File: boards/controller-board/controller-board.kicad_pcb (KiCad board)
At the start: 2 copper layers, 130 x 115 mm, 213 parts, among them IC10 A6214KLKTR-T, IC11 A6214KLKTR-T, IC12 A6214KLKTR-T, IC13 A6214KLKTR-T, IC2 A6214KLKTR-T, IC3 A6214KLKTR-T, IC4 A6214KLKTR-T, IC5 A6214KLKTR-T, IC6 A6214KLKTR-T, IC7 A6214KLKTR-T, IC8 A6214KLKTR-T, IC9 A6214KLKTR-T, J1 Conn_01x02, J2 Conn_01x02, J3 Conn_01x02, J4 Conn_01x02, J5 Conn_01x03, J6 Conn_01x02, Q1 PMV45EN, Q2 Goford_G11S_20V_11A, SW1 EG1271, U1 LTC3624, U2 ADS1015IRUGR, U3 ADS1015IRUGR, U4 RPi_Pico, U5 MCP4728

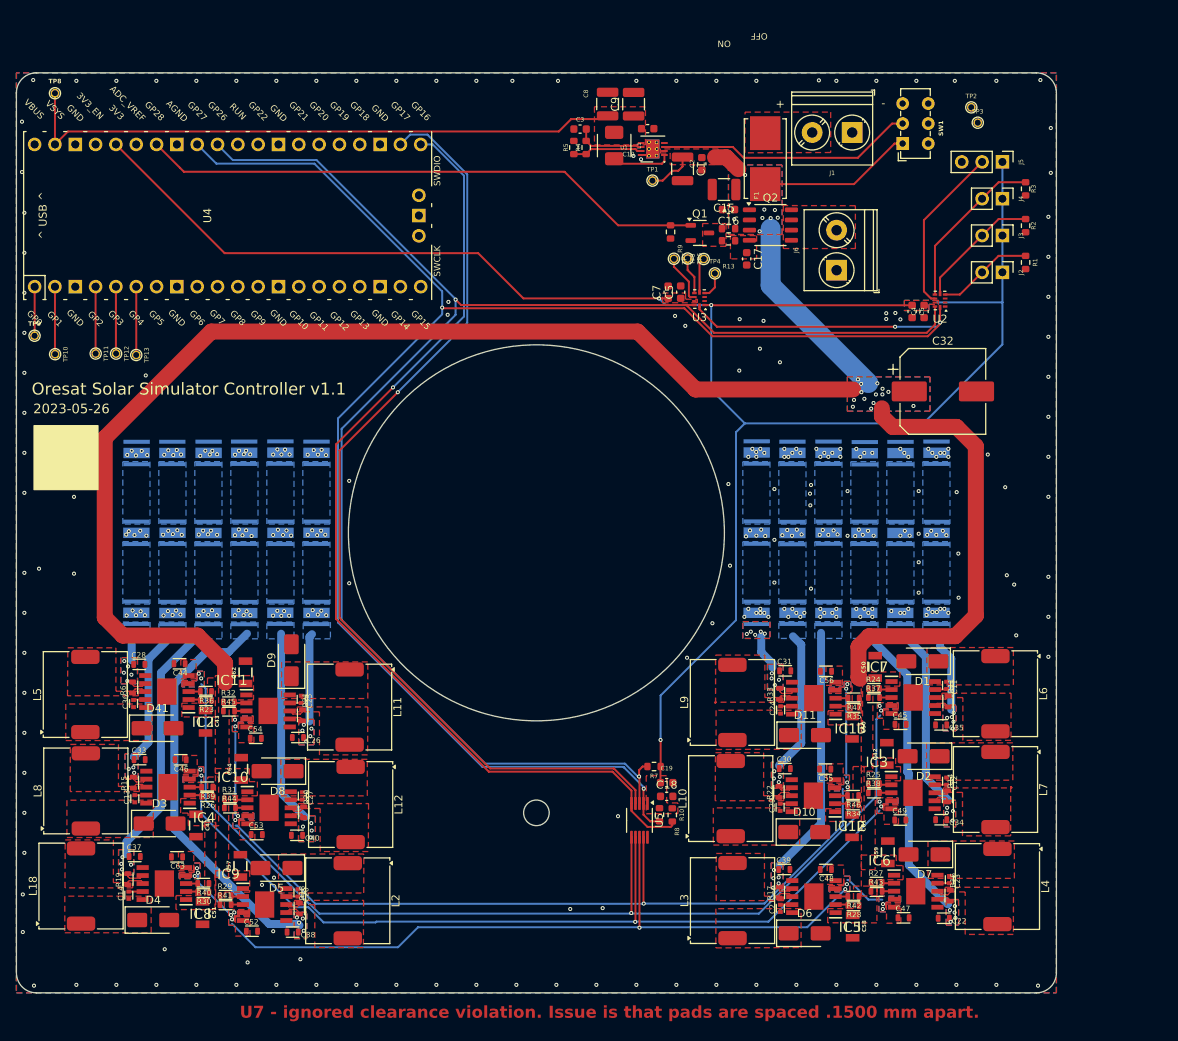
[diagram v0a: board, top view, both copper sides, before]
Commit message: added pull-down resistor to ADIM pins on LED drivers, completed BOM, reorganized schematic, switched 10k resistors and thermistors, added datasheets, split 12V pwr supply and added additional fuse, changed main pwr input connector to one with higher current rating
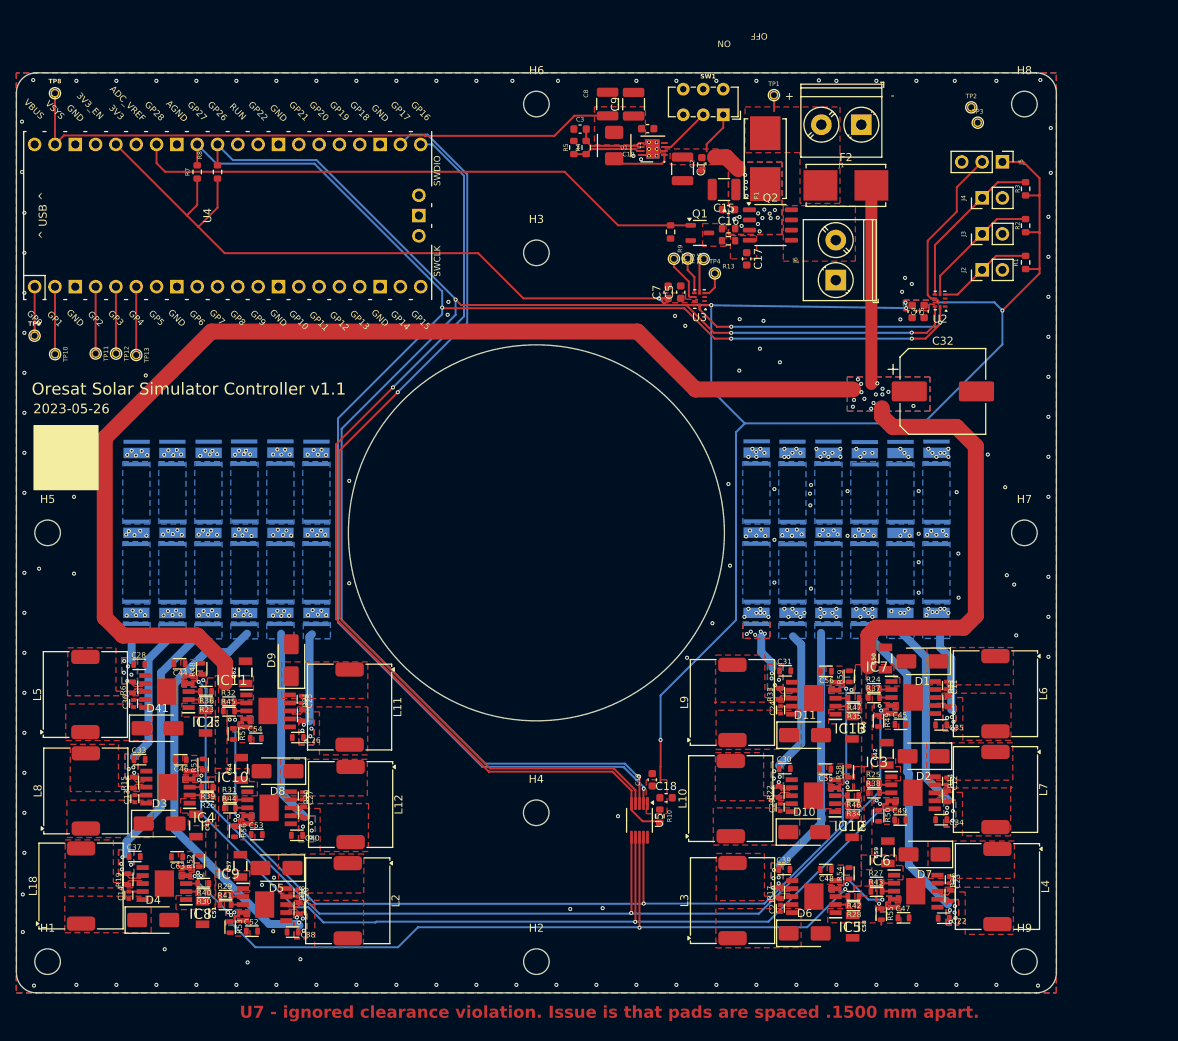
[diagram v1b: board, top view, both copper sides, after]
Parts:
- removed REF**: MountingHole_3.2mm_M3, MountingHole:MountingHole_3.2mm_M3
- added F2: 10A, Fuse:Fuseholder_Littelfuse_Nano2_154x, F.Cu at (183.7, 59.1)
- added H1: MountingHole, oresat-misc:MountingHole_3.2mm_M3, F.Cu at (83.9, 156.1)
- added H2: MountingHole, oresat-misc:MountingHole_3.2mm_M3, F.Cu at (145.0, 156.1)
- added H3: MountingHole, oresat-misc:MountingHole_3.2mm_M3, F.Cu at (145.0, 67.5)
- added H4: MountingHole, oresat-misc:MountingHole_3.2mm_M3, F.Cu at (145.0, 137.5)
- added H5: MountingHole, oresat-misc:MountingHole_3.2mm_M3, F.Cu at (83.9, 102.5)
- added H6: MountingHole, oresat-misc:MountingHole_3.2mm_M3, F.Cu at (145.0, 48.9)
- added H7: MountingHole, oresat-misc:MountingHole_3.2mm_M3, F.Cu at (206.0, 102.5)
- added H8: MountingHole, oresat-misc:MountingHole_3.2mm_M3, F.Cu at (206.0, 48.9)
- added H9: MountingHole, oresat-misc:MountingHole_3.2mm_M3, F.Cu at (206.0, 156.1)
- added R48: 100k, oresat-passives:0603-C, F.Cu at (103.2, 119.5)
- added R49: 100k, oresat-passives:0603-C, F.Cu at (187.8, 126.0)
- added R50: 100k, oresat-passives:0603-C, F.Cu at (187.8, 137.9)
- added R51: 100k, oresat-passives:0603-C, F.Cu at (103.3, 131.5)
- added R52: 100k, oresat-passives:0603-C, F.Cu at (102.8, 143.5)
- added R53: 100k, oresat-passives:0603-C, F.Cu at (106.7, 151.8)
- added R54: 100k, oresat-passives:0603-C, F.Cu at (184.1, 145.0)
- added R55: 100k, oresat-passives:0603-C, F.Cu at (188.1, 150.2)
- added R56: 100k, oresat-passives:0603-C, F.Cu at (107.3, 139.8)
- added R57: 100k, oresat-passives:0603-C, F.Cu at (107.1, 127.6)
- added R58: 100k, oresat-passives:0603-C, F.Cu at (184.0, 132.4)
- added R59: 100k, oresat-passives:0603-C, F.Cu at (184.1, 120.4)
- D47, D48, D49, D50, D51, D52, D53, D54, D55, D56, D57, D58, D59, D60, D61, D62, D63, D64, D71, D72, D73, D74, D75, D76, D77, D78, D79, D80, D81, D82, D83, D84, D85, D86, D87, D88: value XPEBBL-L1-0000-00201 -> LED_Pad
- moved R8 97.5 mm to (105.1, 57.4), turned to 90 degrees
- moved R7 93.7 mm to (102.6, 57.4), turned to 90 degrees
- moved SW1 22.7 mm to (168.4, 50.2), turned to 180 degrees
- moved TP1 18.6 mm to (174.7, 47.8)
- moved J2 2.56 mm to (200.7, 69.6), turned to 90 degrees
- moved J3 2.55 mm to (200.7, 65.1), turned to 90 degrees
- moved J4 2.54 mm to (200.7, 60.6), turned to 90 degrees
- moved C19 1.84 mm to (159.5, 133.4), turned to 90 degrees
- moved C50 1.64 mm to (188.6, 118.2)
- moved R10 1.56 mm to (160.4, 137.9)
- moved J1 1.51 mm to (185.6, 51.5)
- moved J6 1.24 mm to (182.4, 70.9)
- moved C18 0.19 mm to (161.2, 135.6)
- turned R1 to 90 degrees
- turned R2 to 90 degrees
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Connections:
- C1 pad 1: VCC -> +12Vpwm
- C15 pad 1: VCC -> +12Vpwm
- C16 pad 1: VCC -> +12Vpwm
- C2 pad 1: VCC -> +12Vpwm
- C32 pad 1: VCC -> +12V
- C41 pad 1: VCC -> +12V
- C42 pad 1: VCC -> +12V
- C43 pad 1: VCC -> +12V
- C50 pad 1: VCC -> +12V
- C51 pad 1: VCC -> +12V
- C57 pad 1: VCC -> +12V
- C58 pad 1: VCC -> +12V
- C59 pad 1: VCC -> +12V
- C60 pad 1: VCC -> +12V
- C61 pad 1: VCC -> +12V
- C62 pad 1: VCC -> +12V
- C64 pad 1: VCC -> +12V
- F1 pad 2: VCC -> +12Vpwm
- IC10 pad 1: VCC -> +12V
- IC11 pad 1: VCC -> +12V
- IC12 pad 1: VCC -> +12V
- IC13 pad 1: VCC -> +12V
- IC2 pad 1: VCC -> +12V
- IC3 pad 1: VCC -> +12V
- IC4 pad 1: VCC -> +12V
- IC5 pad 1: VCC -> +12V
- IC6 pad 1: VCC -> +12V
- IC7 pad 1: VCC -> +12V
- IC8 pad 1: VCC -> +12V
- IC9 pad 1: VCC -> +12V
- J2 pad 1: +3.3V -> /THERM1
- J2 pad 2: /THERM1 -> GND
- J3 pad 1: +3.3V -> /THERM2
- J3 pad 2: /THERM2 -> GND
- J4 pad 1: +3.3V -> /THERM3
- J4 pad 2: /THERM3 -> GND
- Q2 pad 1: VCC -> +12Vpwm
- Q2 pad 2: VCC -> +12Vpwm
- Q2 pad 3: VCC -> +12Vpwm
- R1 pad 1: /THERM1 -> +3.3V
- R1 pad 2: GND -> /THERM1
- R12 pad 1: VCC -> +12Vpwm
- R2 pad 1: /THERM2 -> +3.3V
- R2 pad 2: GND -> /THERM2
- R23 pad 1: VCC -> +12V
- R24 pad 1: VCC -> +12V
- R25 pad 1: VCC -> +12V
- R26 pad 1: VCC -> +12V
- R27 pad 1: VCC -> +12V
- R28 pad 1: VCC -> +12V
- R29 pad 1: VCC -> +12V
- R3 pad 1: /THERM3 -> +3.3V
- R3 pad 2: GND -> /THERM3
- R30 pad 1: VCC -> +12V
- R31 pad 1: VCC -> +12V
- R32 pad 1: VCC -> +12V
- R34 pad 1: VCC -> +12V
- R35 pad 1: VCC -> +12V
- R36 pad 1: VCC -> +12V
- R37 pad 1: VCC -> +12V
- R38 pad 1: VCC -> +12V
- R39 pad 1: VCC -> +12V
- R40 pad 1: VCC -> +12V
- R41 pad 1: VCC -> +12V
- R42 pad 1: VCC -> +12V
- R43 pad 1: VCC -> +12V
- R44 pad 1: VCC -> +12V
- R45 pad 1: VCC -> +12V
- R46 pad 1: VCC -> +12V
- R47 pad 1: VCC -> +12V
- R7 pad 2: /SDA1 -> /SCL1
- R8 pad 2: /SCL1 -> /SDA1
- SW1 pad 1: VCC -> +12Vpwm
- TP1 pad 1: VCC -> Net-(J1-Pin_2)
- U1 pad 2: VCC -> +12Vpwm
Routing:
- net VCC: track 253.0 -> 0.00 mm, vias 22 -> 0
- net +12V: track 0.00 -> 223.0 mm, vias 0 -> 14
- net Net-(SW1-B): track 32.1 -> 6.53 mm
- net +3.3V: track 243.0 -> 266.5 mm, vias 3 -> 6
- net +12Vpwm: track 0.00 -> 8.98 mm, vias 0 -> 16
- net /DAC_RDY/~{BSY}: track 123.9 -> 121.5 mm
- net Net-(J1-Pin_2): track 0.00 -> 2.01 mm
- net /PWM: track 71.0 -> 72.3 mm
- net /SCL1: track 235.8 -> 234.9 mm, vias 4 -> 6
- net GND: track 1.25 -> 1.88 mm
- net /SDA1: track 199.8 -> 200.4 mm, vias 2 -> 4
- added copper zone on B.Cu, net +12V
- added copper zone on F.Cu, net +12V
- added copper zone on B.Cu, net +12Vpwm
- added copper zone on F.Cu, net +12Vpwm
- removed copper zone on B.Cu, net VCC
- removed copper zone on F.Cu, net VCC

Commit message: minor changes to schematic, pcb, and BOM
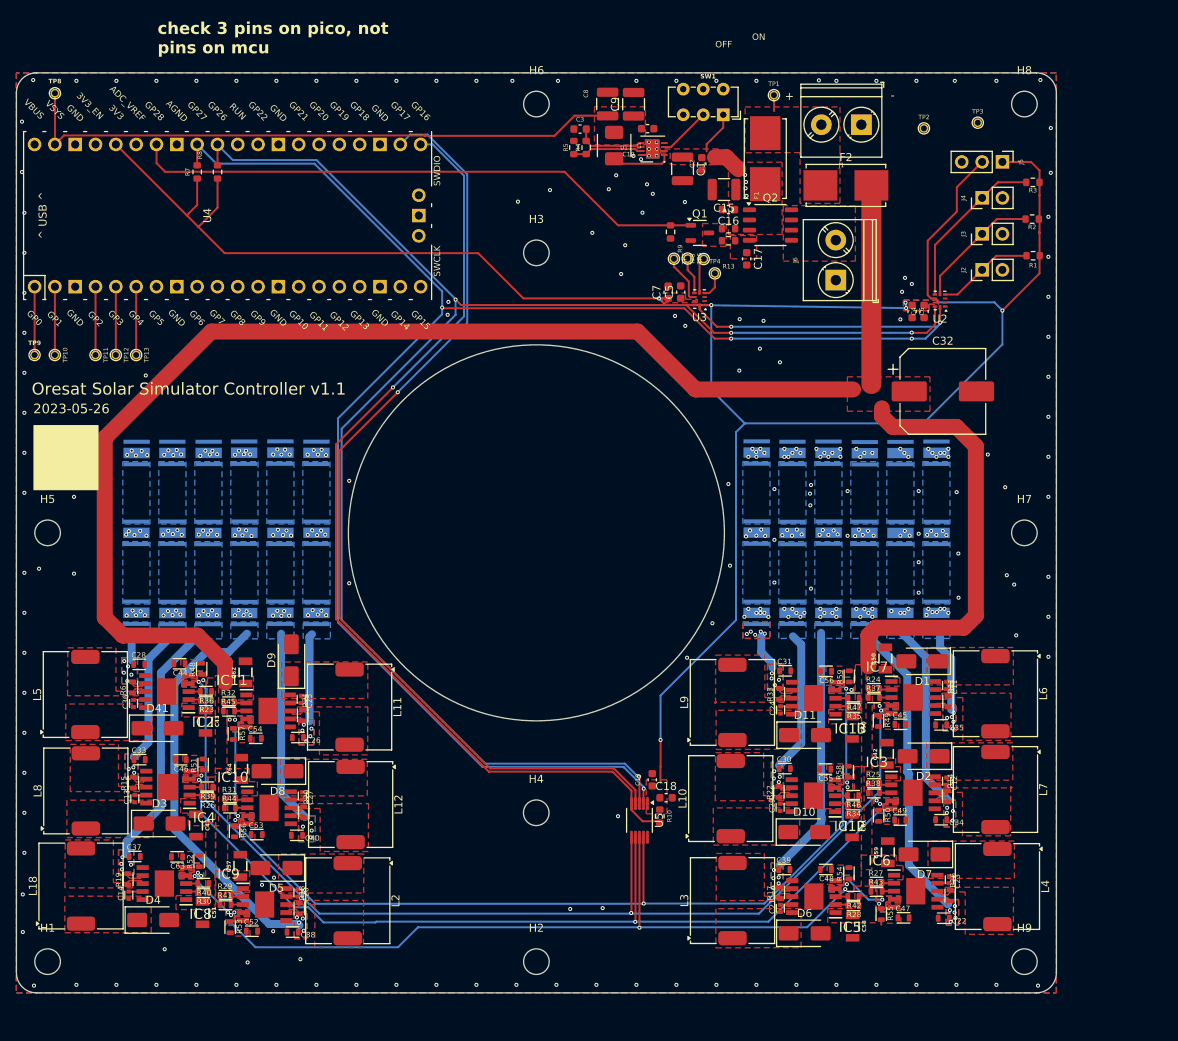
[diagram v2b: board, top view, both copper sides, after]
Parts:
- moved TP2 6.48 mm to (193.4, 51.9)
- moved TP9 2.41 mm to (82.3, 80.3)
- moved R1 1.26 mm to (207.1, 67.9), turned to 180 degrees
- moved R3 1.22 mm to (207.1, 58.7), turned to 180 degrees
- moved R2 1.16 mm to (207.0, 63.3), turned to 180 degrees
- moved TP11 0.18 mm to (89.9, 80.3)
- moved TP12 0.17 mm to (92.4, 80.3)
- moved TP10 0.10 mm to (84.8, 80.3)
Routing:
- net +3.3V: track 266.5 -> 261.9 mm
- net Net-(U4-GPIO0): track 5.72 -> 8.13 mm
- net Net-(U4-GPIO2): track 7.95 -> 8.55 mm
- net Net-(U4-GPIO3): track 7.97 -> 8.54 mm
- net Net-(U4-GPIO1): track 8.04 -> 8.54 mm
- net GND: vias 326 -> 337
- net +12Vpwm: vias 16 -> 4
- net +12V: vias 14 -> 0
- removed copper zone on B.Cu, net +12V
- removed copper zone on B.Cu, net +12Vpwm
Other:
- board text added: "check 3 pins on pico, not pins on mcu"
- board text removed: "U7 - ignored clearance violation. Issue is that pads are spaced .1500 mm apart."

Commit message: removed 100k pull-down resistors from LED drivers and added a 100k resistor to each output of DAC, other misc schematic and pcb changes
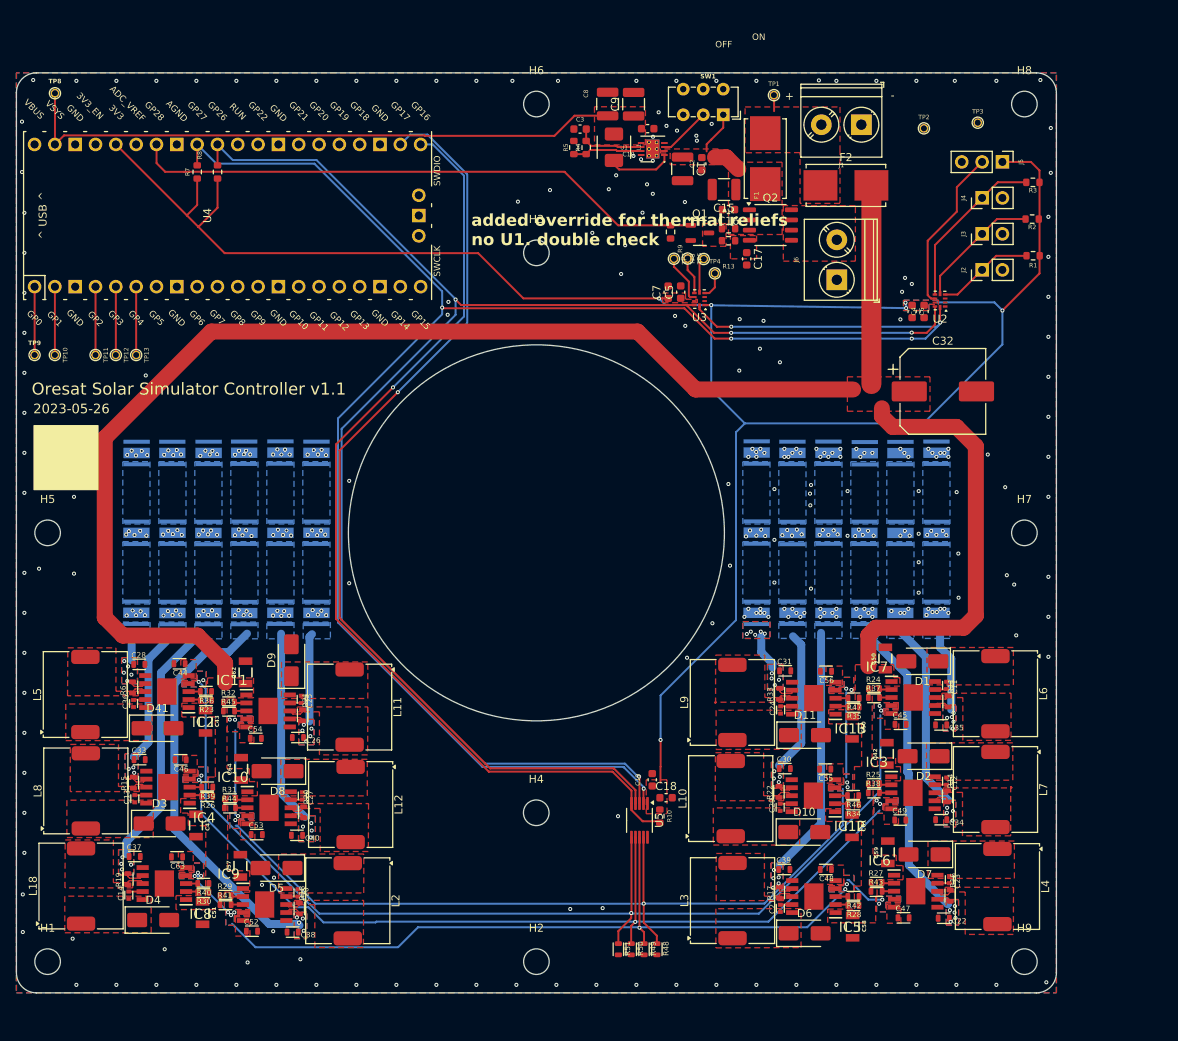
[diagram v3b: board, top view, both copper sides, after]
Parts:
- removed R52, R53, R54, R55, R56, R57, R58, R59: 100k, oresat-passives:0603-C
- D47, D48, D57, D58, D59, D64: value LED_Pad -> XPEBRD-L1-0000-00501
- D49, D50, D51, D52, D60, D61: value LED_Pad -> XPEBGR-L1-0000-00D01
- D53, D54, D55, D56, D62, D63, D71, D72, D73, D74, D83, D84: value LED_Pad -> XPEBBL-L1-0000-00201
- D75, D76, D77, D78, D79, D80, D81, D82, D85, D86, D87, D88: value LED_Pad -> 153283367A212
- F1, F2: value 10A -> 01550900DR
- J6: value Conn_01x02 -> Phoenix 1995499
- R20, R21, R22, R33: value .576 -> 3.4
- moved R48 66.8 mm to (160.1, 154.6), turned to -90 degrees
- moved R51 56.8 mm to (155.2, 154.6), turned to -90 degrees
- moved R49 40.9 mm to (158.5, 154.6)
- moved R50 35.1 mm to (156.8, 154.6)
- moved L1 0.21 mm to (154.7, 54.3)
- moved J6 0.14 mm to (182.6, 70.9)
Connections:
- R48 pad 1: RED_LIM -> UV_LIM
- R49 pad 1: RED_LIM -> BLUE_LIM
- R51 pad 1: GREEN_LIM -> RED_LIM
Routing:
- net UV_LIM: track 118.1 -> 123.8 mm
- net RED_LIM: track 130.5 -> 135.0 mm
- net GREEN_LIM: track 111.0 -> 114.0 mm
- net BLUE_LIM: track 104.6 -> 106.9 mm
- net GND: track 1.88 -> 0.37 mm, vias 337 -> 345
- net Net-(U1-SW): track 7.08 -> 7.94 mm
- net +12Vpwm: vias 4 -> 0
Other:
- board text added: "added override for thermal reliefs no U1. double check"
- board text removed: "check 3 pins on pico, not pins on mcu"

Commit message: minor changes
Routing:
- net GND: vias 345 -> 348
